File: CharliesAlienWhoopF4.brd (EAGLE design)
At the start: 29 x 29 mm, 41 parts, among them M1 53047-0210, M2 53047-0210, M3 53047-0210, M4 53047-0210, Q1 FDMA410NZ, Q2 FDMA410NZ, Q3 IRLML6402, Q4 FDMA410NZ, Q5 FDMA410NZ, U1 MPU-9250, U2 TPS63001, Y1 8mhz

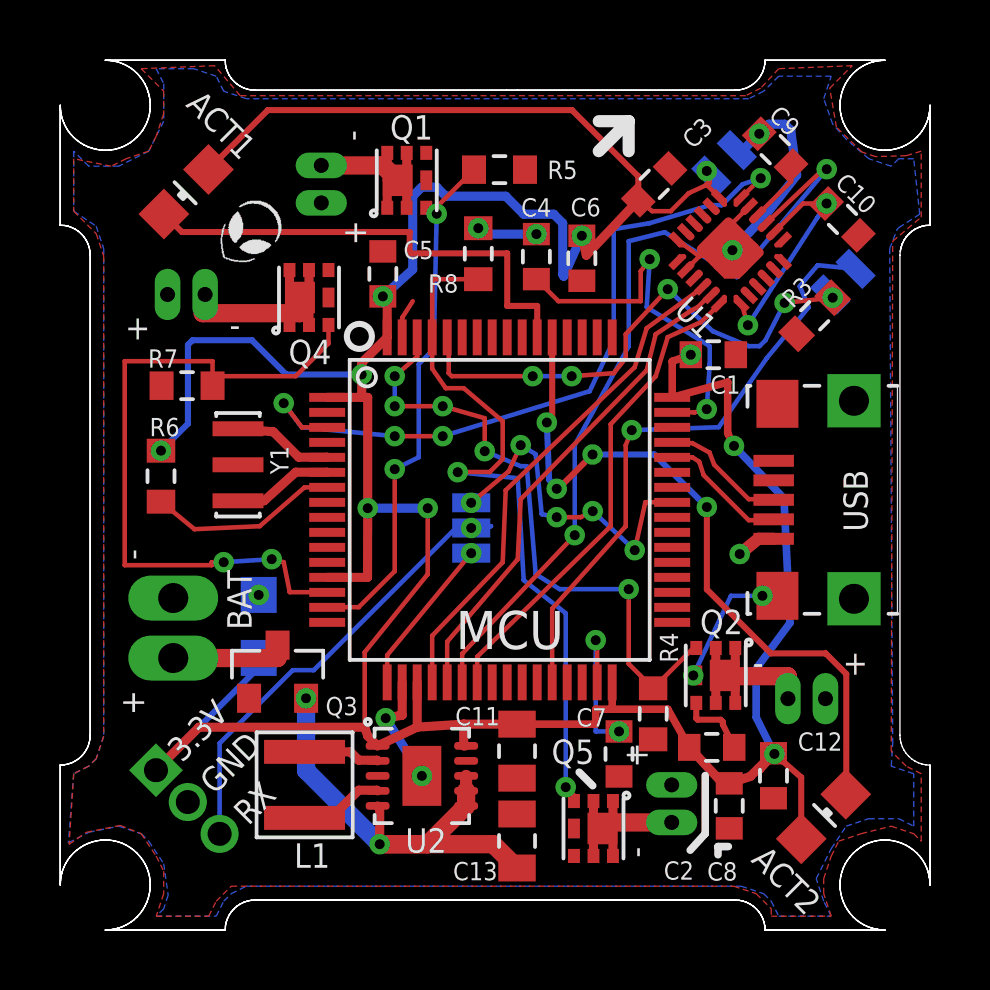
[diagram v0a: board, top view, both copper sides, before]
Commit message: I was having issues with solder bridges underneath the buckboost. Turns out my traces were too wide and when translated into gerber were leaving not much room for error. Hoping this makes reflow success rate 100% ;)
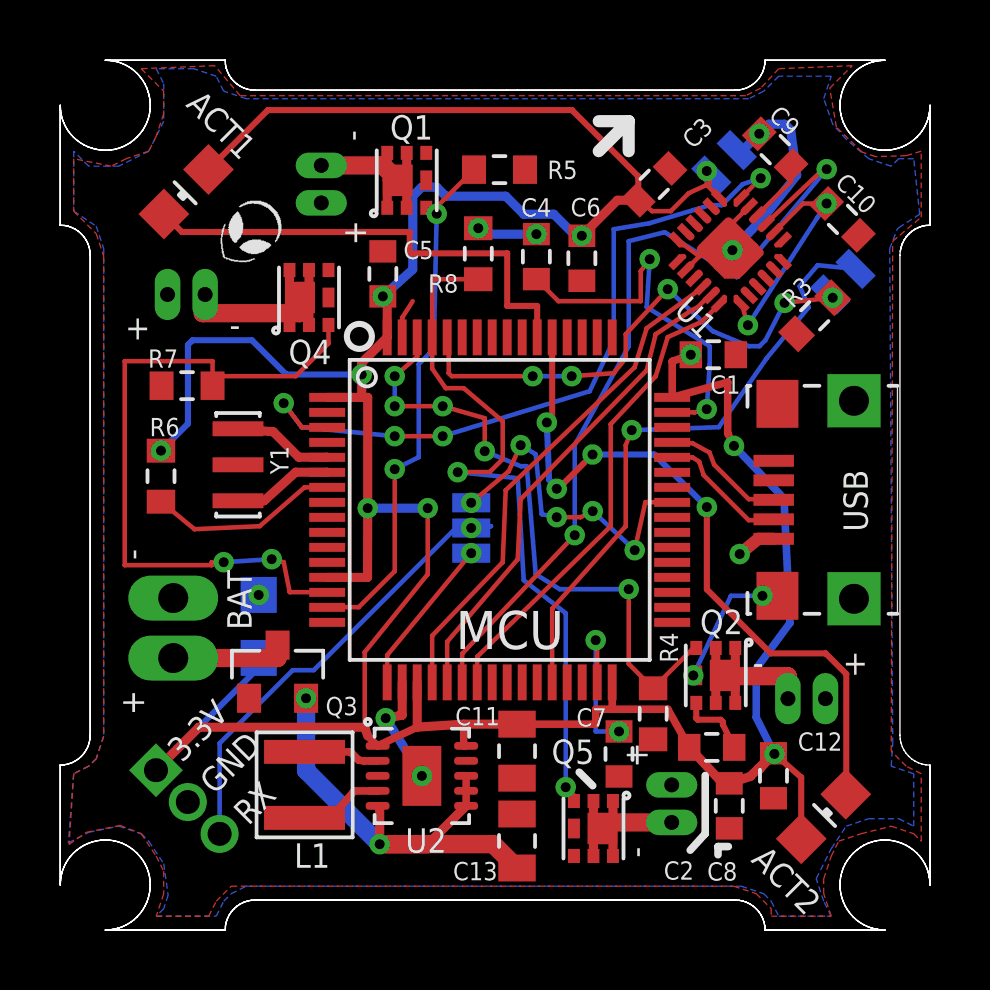
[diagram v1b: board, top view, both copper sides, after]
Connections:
- net N$7 renamed L1
- net N$8 renamed L2
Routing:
- net 3.3V: track 123.3 -> 119.9 mm
